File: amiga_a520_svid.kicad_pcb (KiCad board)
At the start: 2 copper layers, 94 parts, among them J1 Conn_01x16, J10 Y, J11 Y, J12 COMP, J13 COMP, J14 GND, J15 GND, J16 Cr, J17 Cr, J18 LUMA, J19 LUMA, J2 Y, J20 GND, J21 GND, J22 GND, J23 GND, J24 Cb, J25 Cb, J26 CRMA, J27 CRMA, J28 GND, J29 GND, J3 Cr, J30 GND, J31 GND, J4 Cb, J5 COMP, J6 LUMA, J7 CRMA, J8 FU, J9 FU, Q1 2N3906, U1 AD8056ANZ, U2 AD8056ANZ, U3 AD8056ANZ, U4 AD724JRZ-R7

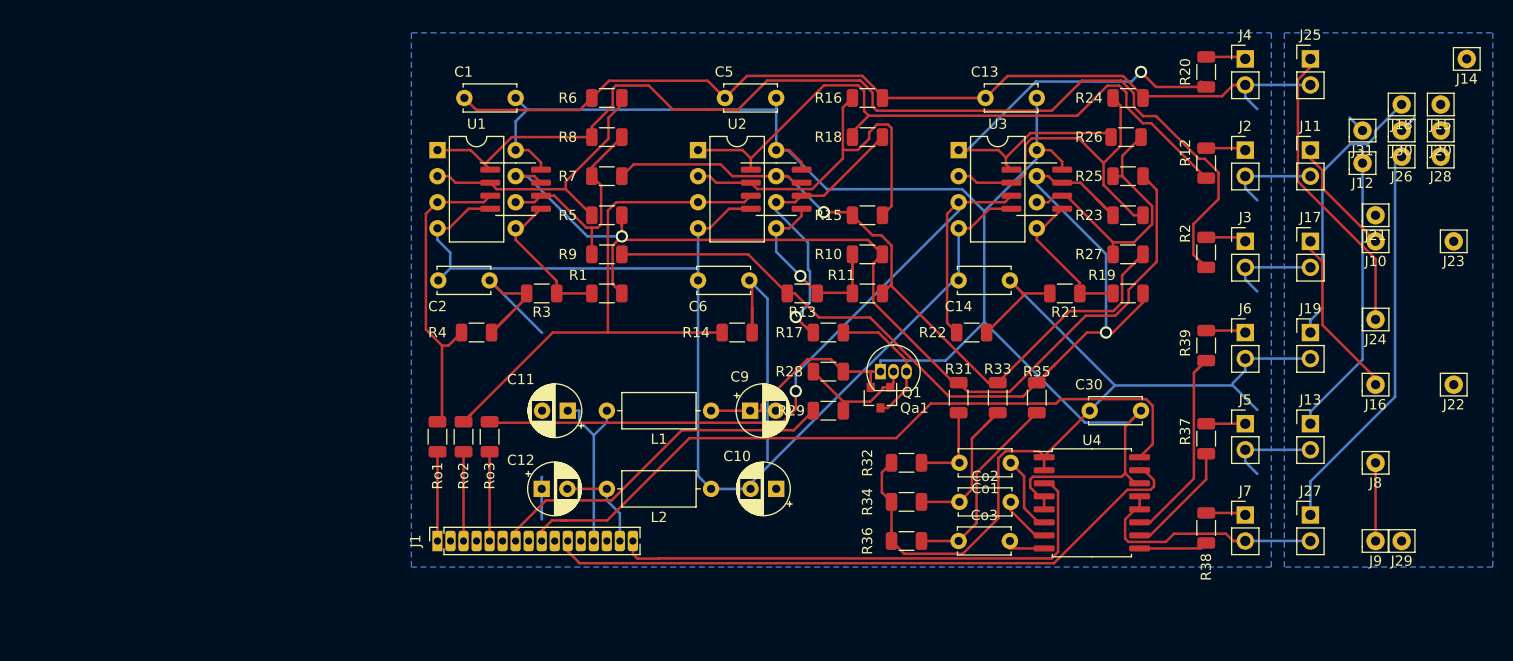
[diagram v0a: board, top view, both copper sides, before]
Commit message: Wider tracks.
Reroute using wider tracks to help with manual board manufacturing. SVG for printing on transfer material. Mirror F_*
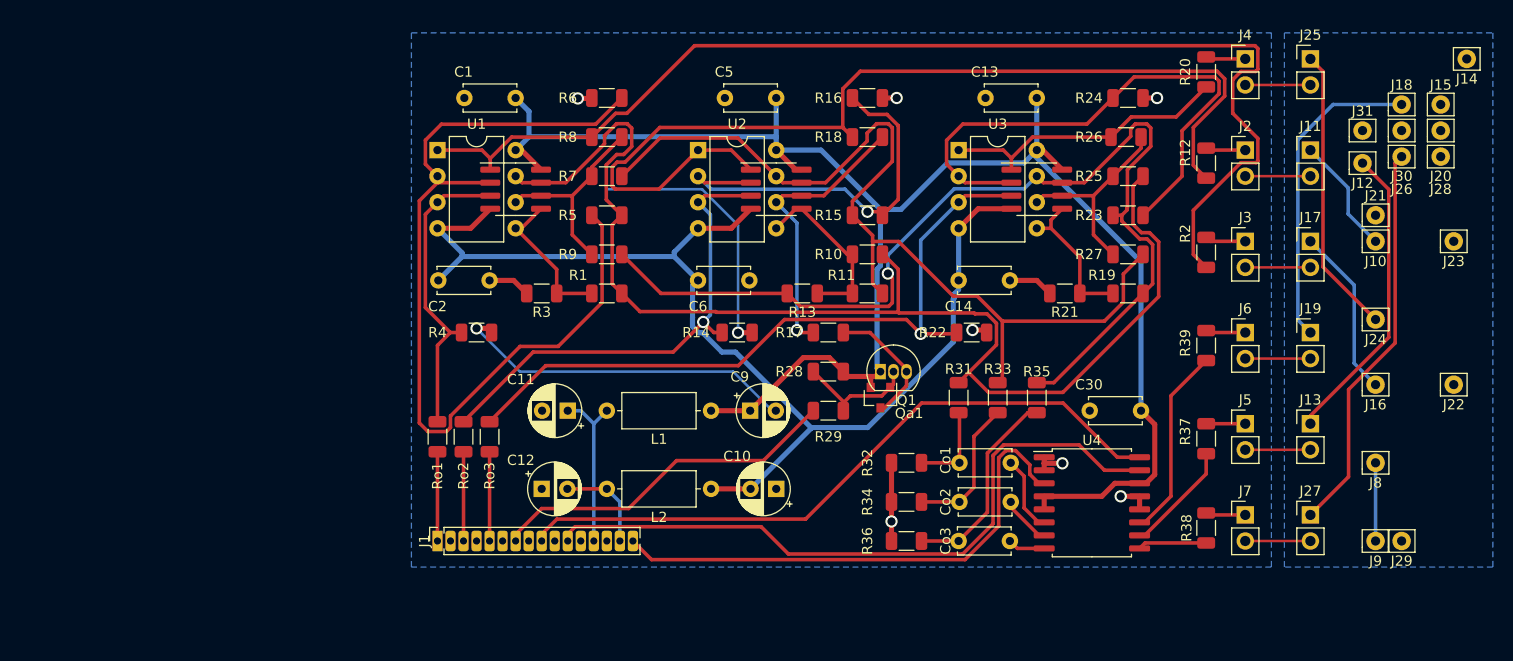
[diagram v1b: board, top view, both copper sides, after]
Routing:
- net GND: track 291.2 -> 126.3 mm, vias 0 -> 9
- net Net-(R5-Pad2): track 28.1 -> 87.7 mm
- net Net-(R12-Pad2): track 65.0 -> 96.7 mm
- net Net-(R23-Pad2): track 33.9 -> 54.8 mm
- net Net-(R20-Pad2): track 46.9 -> 28.5 mm, vias 1 -> 0
- net Rb: track 104.4 -> 121.8 mm, vias 1 -> 0
- net Gb: track 74.7 -> 91.7 mm, vias 1 -> 0
- net Net-(R2-Pad2): track 103.7 -> 114.3 mm
- net Net-(R14-Pad1): track 56.3 -> 47.5 mm, vias 0 -> 1
- net Net-(R25-Pad1): track 26.6 -> 19.9 mm
- net Bb: track 93.0 -> 99.6 mm
- net Net-(R22-Pad1): track 76.1 -> 70.1 mm
- net HSYNC: track 72.1 -> 66.4 mm
- net Net-(R10-Pad1): track 20.9 -> 17.3 mm, vias 1 -> 0
- net Net-(J18-Pad1): track 27.4 -> 30.8 mm
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
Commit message: Fixes after 1st prototype :)
- Swapped OPAMP outputs :(
- More careful AD724 implementation
- MORE SMD! Through hole without metallization is a pain!
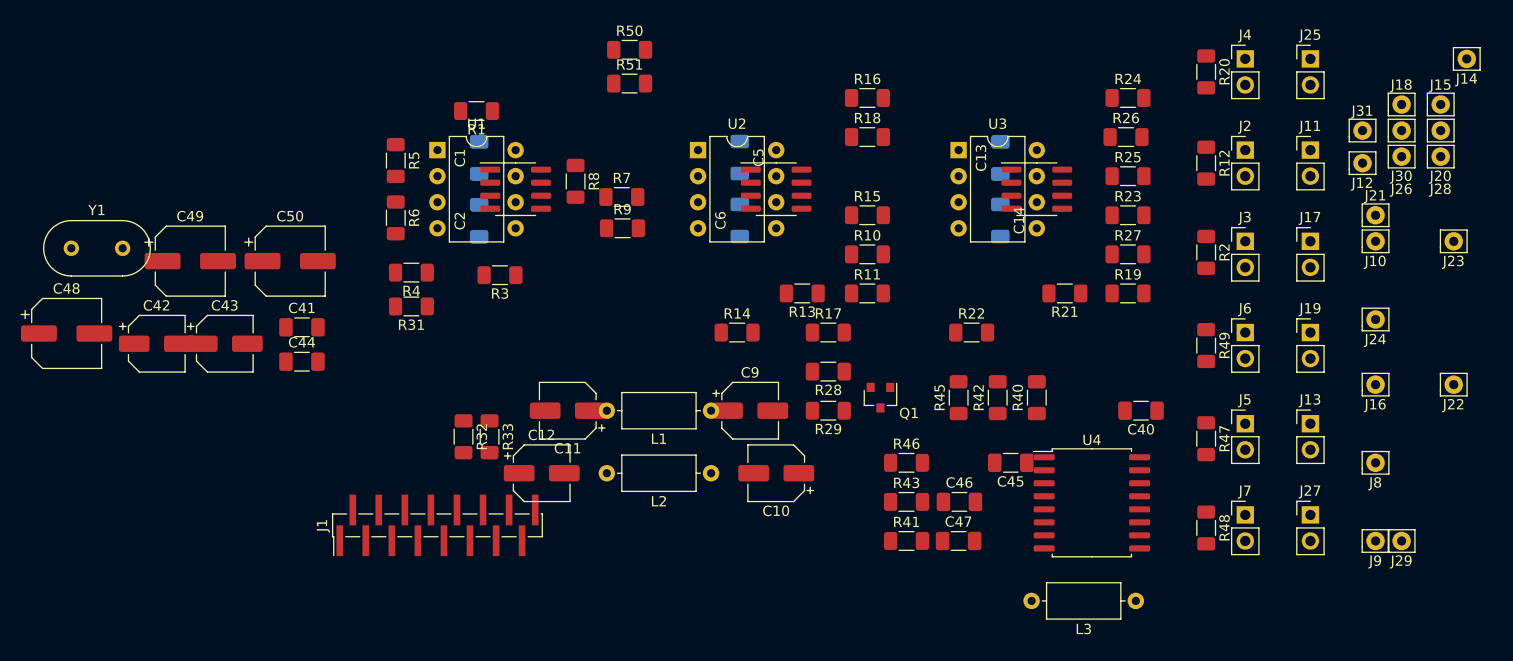
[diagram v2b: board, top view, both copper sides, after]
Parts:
- removed the Q1 at (161.3, 127.0)
- added C41: 100n, Capacitor_SMD:C_1206_3216Metric_Pad1.33x1.80mm_HandSolder, F.Cu at (104.9, 122.7)
- added C42: 10u, Capacitor_SMD:CP_Elec_5x5.4, F.Cu at (90.8, 124.3)
- added C43: 10u, Capacitor_SMD:CP_Elec_5x5.4, F.Cu at (97.4, 124.3)
- added C44: 32p, Capacitor_SMD:C_1206_3216Metric_Pad1.33x1.80mm_HandSolder, F.Cu at (104.9, 126.0)
- added C48: 220u, Capacitor_SMD:CP_Elec_6.3x7.7, F.Cu at (82.0, 123.3)
- added C49: 220u, Capacitor_SMD:CP_Elec_6.3x7.7, F.Cu at (94.0, 116.2)
- added C50: 220u, Capacitor_SMD:CP_Elec_6.3x7.7, F.Cu at (103.8, 116.2)
- added L3: 3.3uH, Inductor_THT:L_Axial_L7.0mm_D3.3mm_P10.16mm_Horizontal_Fastron_MICC, F.Cu at (186.2, 149.4)
- added R50: 5k, Resistor_SMD:R_1206_3216Metric_Pad1.30x1.75mm_HandSolder, F.Cu at (136.8, 95.6)
- added R51: 5k, Resistor_SMD:R_1206_3216Metric_Pad1.30x1.75mm_HandSolder, F.Cu at (136.8, 98.9)
- added Y1: 17.734MHz, Crystal:Resonator-2Pin_W10.0mm_H5.0mm, F.Cu at (82.4, 115.0)
- C1, C13, C14, C2, C5, C6: footprint Capacitor_THT:C_Disc_D5.0mm_W2.5mm_P5.00mm -> Capacitor_SMD:C_1206_3216Metric_Pad1.33x1.80mm_HandSolder; moved to B.Cu
- C10, C11, C12, C9: value 4.7u -> 10u; footprint Capacitor_THT:CP_Radial_D5.0mm_P2.50mm -> Capacitor_SMD:CP_Elec_5x5.4
- C40: renamed from C30; footprint Capacitor_THT:C_Disc_D5.0mm_W2.5mm_P5.00mm -> Capacitor_SMD:C_1206_3216Metric_Pad1.33x1.80mm_HandSolder
- C45: renamed from Co1; footprint Capacitor_THT:C_Disc_D5.0mm_W2.5mm_P5.00mm -> Capacitor_SMD:C_1206_3216Metric_Pad1.33x1.80mm_HandSolder
- C46: renamed from Co2; footprint Capacitor_THT:C_Disc_D5.0mm_W2.5mm_P5.00mm -> Capacitor_SMD:C_1206_3216Metric_Pad1.33x1.80mm_HandSolder
- C47: renamed from Co3; footprint Capacitor_THT:C_Disc_D5.0mm_W2.5mm_P5.00mm -> Capacitor_SMD:C_1206_3216Metric_Pad1.33x1.80mm_HandSolder
- J1: footprint Connector_PinSocket_1.27mm:PinSocket_1x16_P1.27mm_Vertical -> Connector_PinHeader_1.27mm:PinHeader_1x16_P1.27mm_Vertical_SMD_Pin1Left
- L1, L2: value 1k@100MHz -> 3.3uH
- R1, R10, R11, R12, R13, R14, R15, R16, R17, R18, R19, R2, R20, R21, R22, R23, R24, R25, R26, R27, R28, R29, R3, R4, R5, R6, R7, R8, R9: footprint Resistor_SMD:R_1206_3216Metric -> Resistor_SMD:R_1206_3216Metric_Pad1.30x1.75mm_HandSolder
- R31: renamed from Ro1; footprint Resistor_SMD:R_1206_3216Metric -> Resistor_SMD:R_1206_3216Metric_Pad1.30x1.75mm_HandSolder
- R32: renamed from Ro2; footprint Resistor_SMD:R_1206_3216Metric -> Resistor_SMD:R_1206_3216Metric_Pad1.30x1.75mm_HandSolder
- R33: renamed from Ro3; footprint Resistor_SMD:R_1206_3216Metric -> Resistor_SMD:R_1206_3216Metric_Pad1.30x1.75mm_HandSolder
- R40: renamed from R35; value 1k -> 200; footprint Resistor_SMD:R_1206_3216Metric -> Resistor_SMD:R_1206_3216Metric_Pad1.30x1.75mm_HandSolder
- R41: renamed from R36; value 1k -> 200; footprint Resistor_SMD:R_1206_3216Metric -> Resistor_SMD:R_1206_3216Metric_Pad1.30x1.75mm_HandSolder
- R42: renamed from R33; value 1k -> 200; footprint Resistor_SMD:R_1206_3216Metric -> Resistor_SMD:R_1206_3216Metric_Pad1.30x1.75mm_HandSolder
- R43: renamed from R34; value 1k -> 200; footprint Resistor_SMD:R_1206_3216Metric -> Resistor_SMD:R_1206_3216Metric_Pad1.30x1.75mm_HandSolder
- R45: renamed from R31; value 1k -> 200; footprint Resistor_SMD:R_1206_3216Metric -> Resistor_SMD:R_1206_3216Metric_Pad1.30x1.75mm_HandSolder
- R46: renamed from R32; value 1k -> 200; footprint Resistor_SMD:R_1206_3216Metric -> Resistor_SMD:R_1206_3216Metric_Pad1.30x1.75mm_HandSolder
- R47: renamed from R37; footprint Resistor_SMD:R_1206_3216Metric -> Resistor_SMD:R_1206_3216Metric_Pad1.30x1.75mm_HandSolder
- R48: renamed from R38; footprint Resistor_SMD:R_1206_3216Metric -> Resistor_SMD:R_1206_3216Metric_Pad1.30x1.75mm_HandSolder
- R49: renamed from R39; footprint Resistor_SMD:R_1206_3216Metric -> Resistor_SMD:R_1206_3216Metric_Pad1.30x1.75mm_HandSolder
- moved R6 23.7 mm to (114.0, 112.0), turned to 270 degrees
- moved R1 21.8 mm to (121.9, 101.6), turned to 180 degrees
- moved R5 21.3 mm to (114.0, 106.4), turned to 270 degrees
- moved R31 13.0 mm to (115.6, 120.7), turned to 180 degrees
- moved R4 8.63 mm to (115.6, 117.3), turned to 180 degrees
- moved C6 7.12 mm to (147.6, 112.3), turned to 270 degrees
- moved C14 7.12 mm to (173.0, 112.3), turned to 90 degrees
- moved C2 7.04 mm to (122.2, 112.3), turned to 270 degrees
- moved C13 6.84 mm to (173.0, 106.2), turned to 270 degrees
- moved C1 6.84 mm to (122.2, 106.2), turned to 270 degrees
- moved C5 6.81 mm to (147.6, 106.1), turned to 90 degrees
- moved R8 5.29 mm to (131.6, 108.5), turned to 270 degrees
- moved R3 4.44 mm to (124.2, 117.6)
- moved R9 2.96 mm to (136.1, 113.0)
- moved R7 2.50 mm to (136.1, 110.0)
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- renumbered Qa1 to Q1
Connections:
- net -5V renamed -12V
- net Net-(C11-Pad1) renamed VDC
- net Net-(J1-Pad1) renamed /R
- C45 pad 1: Net-(Co1-Pad1) -> Net-(C45-Pad1)
- C45 pad 2: Net-(Co1-Pad2) -> Net-(C45-Pad2)
- C47 pad 1: Net-(Co3-Pad1) -> Net-(C47-Pad1)
- C47 pad 2: Net-(Co3-Pad2) -> Net-(C47-Pad2)
- J1 pad 16: BURST -> Net-(J1-Pad16)
- R40 pad 1: Net-(Co3-Pad1) -> Net-(C45-Pad1)
- R41 pad 2: Net-(Co3-Pad1) -> Net-(C45-Pad1)
- R45 pad 1: Net-(Co1-Pad2) -> Net-(C47-Pad1)
- R46 pad 2: Net-(Co1-Pad2) -> Net-(C47-Pad1)
- R47 pad 2: Net-(R37-Pad2) -> Net-(C48-Pad2)
- R48 pad 2: Net-(R38-Pad2) -> Net-(C49-Pad2)
- R49 pad 2: Net-(R39-Pad2) -> Net-(C50-Pad2)
- U1 pad 1: Net-(R2-Pad2) -> Rb
- U1 pad 7: Rb -> Net-(R2-Pad2)
- U2 pad 1: Net-(R12-Pad2) -> Gb
- U2 pad 7: Gb -> Net-(R12-Pad2)
- U3 pad 1: Net-(R20-Pad2) -> Bb
- U3 pad 7: Bb -> Net-(R20-Pad2)
- U4 pad 10: Net-(R37-Pad2) -> Net-(C48-Pad1)
- U4 pad 11: Net-(R39-Pad2) -> Net-(C50-Pad1)
- U4 pad 12: GND -> Net-(R50-Pad1)
- U4 pad 14: +5V -> Net-(C41-Pad1)
- U4 pad 3: BURST -> Net-(C44-Pad2)
- U4 pad 5: +5V -> Net-(R51-Pad1)
- U4 pad 6: Net-(Co1-Pad1) -> Net-(C47-Pad2)
- U4 pad 8: Net-(Co3-Pad2) -> Net-(C45-Pad2)
- U4 pad 9: Net-(R38-Pad2) -> Net-(C49-Pad1)
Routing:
- net +5V: track 166.3 -> 0.00 mm
- net GND: track 126.3 -> 0.00 mm, vias 9 -> 0
- net Rb: track 121.8 -> 0.00 mm
- net Net-(R2-Pad2): track 114.3 -> 0.00 mm
- net -12V: track 113.8 -> 0.00 mm
- net Bb: track 99.6 -> 0.00 mm, vias 1 -> 0
- net Net-(R12-Pad2): track 96.7 -> 0.00 mm
- net Gb: track 91.7 -> 0.00 mm
- net Net-(R5-Pad2): track 87.7 -> 0.00 mm
- net Net-(R22-Pad1): track 70.1 -> 0.00 mm, vias 1 -> 0
- net VSYNC: track 67.1 -> 0.00 mm
- net HSYNC: track 66.4 -> 0.00 mm
- net Net-(R23-Pad2): track 54.8 -> 0.00 mm
- net BURST: track 51.0 -> 0.00 mm
- net Net-(R14-Pad1): track 47.5 -> 0.00 mm, vias 1 -> 0
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- removed copper zone on B.Cu, net GND
